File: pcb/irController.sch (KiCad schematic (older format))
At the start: 29 parts, among them J1 B4B-PH-K-S(LF)(SN), P1 ZX62R-B-5P, P2 GPIO_USER, Q1 Q_NMOS, SW1 SKRPACE010, SW2 SKRPACE010, U1 NJM2845, U2 ESP-13-WROOM-02, U3 IRSNS_GP1UXC41QS

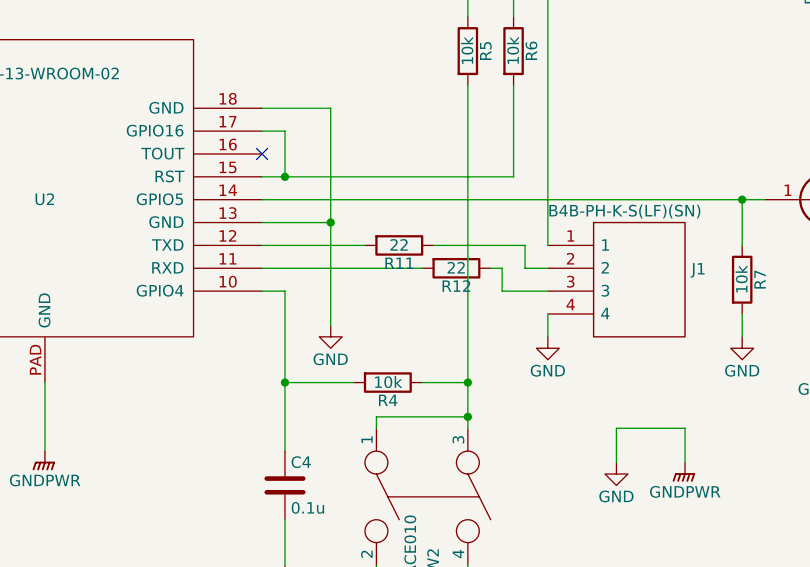
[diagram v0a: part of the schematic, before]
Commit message: 通信線の誤配線を修正
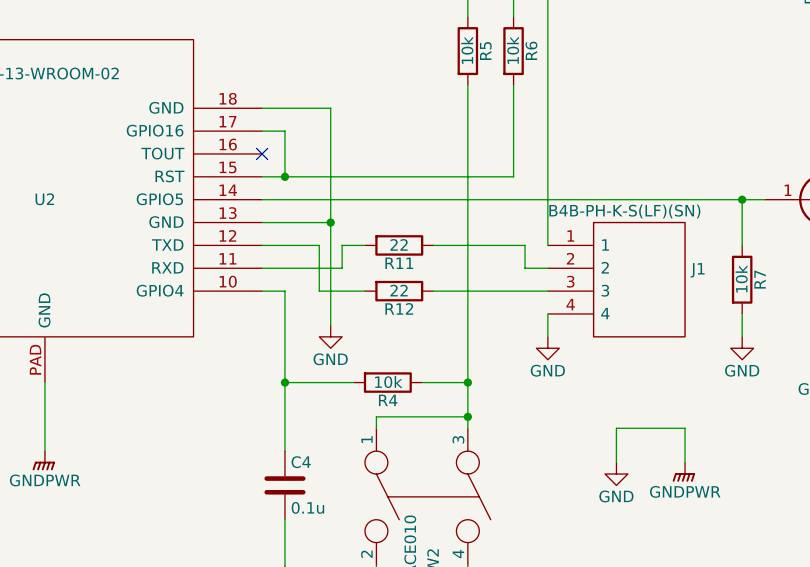
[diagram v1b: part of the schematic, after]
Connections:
- wire segments 115 -> 117
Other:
- moved on the sheet: R12
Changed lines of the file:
@@
 	6900 3600 9000 3600
-Wire Wire Line
-	6900 3900 7600 3900
 Wire Wire Line
 	2850 3200 2900 3200
@@
 $EndComp
 Wire Wire Line
-	8150 4000 7950 4000
-Wire Wire Line
-	7950 4000 7950 3900
-Wire Wire Line
 	8150 3900 8050 3900
 Wire Wire Line
@@
 Wire Wire Line
 	7200 3700 7200 4150
-Wire Wire Line
-	6900 3800 7350 3800
 Wire Wire Line
 	7650 3800 8050 3800
@@
 	0    1    1    0
 $EndComp
-$Comp
-L irController-rescue:R R12
-U 1 1 5E13E423
-P 7750 3900
-F 0 "R12" V 7830 3900 50  0000 C CNN
-F 1 "22" V 7750 3900 50  0000 C CNN
-F 2 "Resistor_SMD:R_0603_1608Metric" V 7680 3900 50  0001 C CNN
-F 3 "" H 7750 3900 50  0000 C CNN
-	1    7750 3900
-	0    1    1    0
-$EndComp
-Wire Wire Line
-	7900 3900 7950 3900
 Wire Wire Line
 	7300 4400 7000 4400
@@
 Wire Wire Line
 	3750 3900 3350 3900
+Wire Wire Line
+	6900 3800 7150 3800
+$Comp
+L irController-rescue:R R12
+U 1 1 5E13E423
+P 7500 4000
+F 0 "R12" V 7580 4000 50  0000 C CNN
+F 1 "22" V 7500 4000 50  0000 C CNN
+F 2 "Resistor_SMD:R_0603_1608Metric" V 7430 4000 50  0001 C CNN
+F 3 "" H 7500 4000 50  0000 C CNN
+	1    7500 4000
+	0    1    1    0
+$EndComp
+Wire Wire Line
+	7650 4000 8150 4000
+Wire Wire Line
+	7150 4000 7350 4000
+Wire Wire Line
+	7150 3800 7150 4000
+Wire Wire Line
+	6900 3900 7250 3900
+Wire Wire Line
+	7250 3900 7250 3800
+Wire Wire Line
+	7250 3800 7350 3800
 $EndSCHEMATC

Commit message: 温度センサ搭載
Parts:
- removed P2: GPIO_USER, Socket_Strips:Socket_Strip_Straight_1x02, symbol irController-rescue:CONN_01X02
- added C5: 0.1u, Capacitors_SMD:C_0603, symbol irController-rescue:C
- added IC1: ADT7410TRZ, SOIC127P600X175-8N, symbol SamacSys:ADT7410TRZ
- added R14, R15, R16, R17: 10k, Resistor_SMD:R_0603_1608Metric, symbol irController-rescue:R
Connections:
- net labels added: +3V3
- wire segments 117 -> 151
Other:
- note added: "I2C Bus Address Options\nA0: L\nA1: L\naddress: 0x48"
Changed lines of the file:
@@
 	1    0    0    -1
-$EndComp
-$Comp
-L irController-rescue:CONN_01X02 P2
-U 1 1 585CF068
-P 4050 3550
-F 0 "P2" H 4050 3750 50  0000 C CNN
-F 1 "GPIO_USER" V 4150 3550 50  0000 C CNN
-F 2 "Socket_Strips:Socket_Strip_Straight_1x02" H 4050 3550 50  0001 C CNN
-F 3 "" H 4050 3550 50  0000 C CNN
-	1    4050 3550
-	-1   0    0    1
 $EndComp
 NoConn ~ 6900 3400
@@
 Connection ~ 9700 3350
 Wire Wire Line
-	3100 2300 7800 2300
-Wire Wire Line
 	9400 2300 9400 2500
 Connection ~ 8000 2300
@@
 	3650 3200 3650 3350
 Wire Wire Line
-	4250 3500 4950 3500
-Wire Wire Line
-	4950 3600 4250 3600
-Wire Wire Line
 	4400 4000 4400 3700
 Wire Wire Line
@@
 	7200 3200 7200 3700
 Wire Wire Line
-	3100 3200 3100 2300
+	3100 3200 3100 2900
 Connection ~ 3100 3200
 Wire Wire Line
@@
 Wire Wire Line
 	7800 2800 7800 2300
-Connection ~ 7800 2300
 Wire Wire Line
 	7800 3100 7800 4400
@@
 Wire Wire Line
 	7000 3500 8000 3500
-Wire Wire Line
-	3650 3200 4500 3200
 Wire Wire Line
 	3350 3900 3350 4000
@@
 Wire Wire Line
 	7250 3800 7350 3800
+$Comp
+L SamacSys:ADT7410TRZ IC1
+U 1 1 5E806B94
+P 4550 1600
+F 0 "IC1" H 5050 1865 50  0000 C CNN
+F 1 "ADT7410TRZ" H 5050 1774 50  0000 C CNN
+F 2 "SOIC127P600X175-8N" H 5400 1700 50  0001 L CNN
+F 3 "http://componentsearchengine.com/Datasheets/3/ADT7410TRZ.pdf" H 5400 1600 50  0001 L CNN
+F 4 "I2C Temperature Sensor" H 5400 1500 50  0001 L CNN "Description"
+F 5 "1.75" H 5400 1400 50  0001 L CNN "Height"
+F 6 "Analog Devices" H 5400 1300 50  0001 L CNN "Manufacturer_Name"
+F 7 "ADT7410TRZ" H 5400 1200 50  0001 L CNN "Manufacturer_Part_Number"
+F 8 "584-ADT7410TRZ" H 5400 1100 50  0001 L CNN "Mouser Part Number"
+F 9 "https://www.mouser.com/Search/Refine.aspx?Keyword=584-ADT7410TRZ" H 5400 1000 50  0001 L CNN "Mouser Price/Stock"
+F 10 "7591890P" H 5400 900 50  0001 L CNN "RS Part Number"
+F 11 "http://uk.rs-online.com/web/p/products/7591890P" H 5400 800 50  0001 L CNN "RS Price/Stock"
+	1    4550 1600
+	1    0    0    -1
+$EndComp
+Wire Wire Line
+	5550 1700 5950 1700
+Wire Wire Line
+	3650 3200 4500 3200
+Wire Wire Line
+	3850 1600 3850 3600
+Wire Wire Line
+	3850 3600 4950 3600
+Wire Wire Line
+	3950 1700 3950 3500
+Wire Wire Line
+	3950 3500 4950 3500
+$Comp
+L power:+3V3 #PWR0101
+U 1 1 5E82A6D6
+P 3100 2900
+F 0 "#PWR0101" H 3100 2750 50  0001 C CNN
+F 1 "+3V3" H 3115 3073 50  0000 C CNN
+F 2 "" H 3100 2900 50  0001 C CNN
+F 3 "" H 3100 2900 50  0001 C CNN
+	1    3100 2900
+	1    0    0    -1
+$EndComp
+$Comp
+L power:+3V3 #PWR0102
+U 1 1 5E82BE3B
+P 7800 2050
+F 0 "#PWR0102" H 7800 1900 50  0001 C CNN
+F 1 "+3V3" H 7815 2223 50  0000 C CNN
+F 2 "" H 7800 2050 50  0001 C CNN
+F 3 "" H 7800 2050 50  0001 C CNN
+	1    7800 2050
+	1    0    0    -1
+$EndComp
+$Comp
+L power:+3V3 #PWR0103
+U 1 1 5E82C6A0
+P 6000 900
+F 0 "#PWR0103" H 6000 750 50  0001 C CNN
+F 1 "+3V3" H 6015 1073 50  0000 C CNN
+F 2 "" H 6000 900 50  0001 C CNN
+F 3 "" H 6000 900 50  0001 C CNN
+	1    6000 900
+	1    0    0    -1
+$EndComp
+Wire Wire Line
+	7800 2050 7800 2300
+Connection ~ 7800 2300
+$Comp
+L irController-rescue:GND #PWR0104
+U 1 1 5E835B5C
+P 5950 2000
+F 0 "#PWR0104" H 5950 1750 50  0001 C CNN
+F 1 "GND" H 5950 1850 50  0000 C CNN
+F 2 "" H 5950 2000 50  0000 C CNN
+F 3 "" H 5950 2000 50  0000 C CNN
+	1    5950 2000
+	1    0    0    -1
+$EndComp
+Wire Wire Line
+	5950 1700 5950 1950
+$Comp
+L irController-rescue:C C5
+U 1 1 5E8551FE
+P 6250 1750
+F 0 "C5" H 6275 1850 50  0000 L CNN
+F 1 "0.1u" H 6275 1650 50  0000 L CNN
+F 2 "Capacitors_SMD:C_0603" H 6288 1600 50  0001 C CNN
+F 3 "" H 6250 1750 50  0000 C CNN
+	1    6250 1750
+	1    0    0    -1
+$EndComp
+Wire Wire Line
+	6250 1900 6250 1950
+Wire Wire Line
+	6250 1950 5950 1950
+Connection ~ 5950 1950
+Wire Wire Line
+	5950 1950 5950 2000
+Wire Wire Line
+	5550 1600 6000 1600
+Wire Wire Line
+	6000 900  6000 1000
+Connection ~ 6000 1600
+Wire Wire Line
+	6000 1600 6250 1600
+$Comp
+L irController-rescue:GND #PWR0105
+U 1 1 5E873BF2
+P 4250 2100
+F 0 "#PWR0105" H 4250 1850 50  0001 C CNN
+F 1 "GND" H 4250 1950 50  0000 C CNN
+F 2 "" H 4250 2100 50  0000 C CNN
+F 3 "" H 4250 2100 50  0000 C CNN
+	1    4250 2100
+	1    0    0    -1
+$EndComp
+Wire Wire Line
+	4550 1800 4250 1800
+Wire Wire Line
+	4250 1800 4250 1900
+Wire Wire Line
+	4550 1900 4250 1900
+Connection ~ 4250 1900
+Wire Wire Line
+	4250 1900 4250 2100
+Text Notes 4500 1250 0    50   ~ 0
+I2C Bus Address Options\nA0: L\nA1: L\naddress: 0x48
+Connection ~ 4250 1700
+Connection ~ 4000 1600
+Wire Wire Line
+	4250 1700 3950 1700
+Wire Wire Line
+	4550 1700 4250 1700
+Wire Wire Line
+	4000 1600 3850 1600
+Wire Wire Line
+	4550 1600 4000 1600
+Wire Wire Line
+	4000 1100 4000 1200
+Connection ~ 4000 1100
+Wire Wire Line
+	4250 1100 4250 1200
+Wire Wire Line
+	4000 1100 4250 1100
+Wire Wire Line
+	4000 1000 4000 1100
+$Comp
+L power:+3V3 #PWR0106
+U 1 1 5E84A991
+P 4000 1000
+F 0 "#PWR0106" H 4000 850 50  0001 C CNN
+F 1 "+3V3" H 4015 1173 50  0000 C CNN
+F 2 "" H 4000 1000 50  0001 C CNN
+F 3 "" H 4000 1000 50  0001 C CNN
+	1    4000 1000
+	1    0    0    -1
+$EndComp
+Wire Wire Line
+	4250 1500 4250 1700
+Wire Wire Line
+	4000 1500 4000 1600
+$Comp
+L irController-rescue:R R15
+U 1 1 5E840B76
+P 4250 1350
+F 0 "R15" V 4330 1350 50  0000 C CNN
+F 1 "10k" V 4250 1350 50  0000 C CNN
+F 2 "Resistor_SMD:R_0603_1608Metric" V 4180 1350 50  0001 C CNN
+F 3 "" H 4250 1350 50  0000 C CNN
+	1    4250 1350
+	1    0    0    -1
+$EndComp
+$Comp
+L irController-rescue:R R14
+U 1 1 5E83AB10
+P 4000 1350
+F 0 "R14" V 4080 1350 50  0000 C CNN
+F 1 "10k" V 4000 1350 50  0000 C CNN
+F 2 "Resistor_SMD:R_0603_1608Metric" V 3930 1350 50  0001 C CNN
+F 3 "" H 4000 1350 50  0000 C CNN
+	1    4000 1350
+	1    0    0    -1
+$EndComp
+$Comp
+L irController-rescue:R R16
+U 1 1 5E893838
+P 5600 1300
+F 0 "R16" V 5680 1300 50  0000 C CNN
+F 1 "10k" V 5600 1300 50  0000 C CNN
+F 2 "Resistor_SMD:R_0603_1608Metric" V 5530 1300 50  0001 C CNN
+F 3 "" H 5600 1300 50  0000 C CNN
+	1    5600 1300
+	1    0    0    -1
+$EndComp
+$Comp
+L irController-rescue:R R17
+U 1 1 5E893E34
+P 5800 1300
+F 0 "R17" V 5880 1300 50  0000 C CNN
+F 1 "10k" V 5800 1300 50  0000 C CNN
+F 2 "Resistor_SMD:R_0603_1608Metric" V 5730 1300 50  0001 C CNN
+F 3 "" H 5800 1300 50  0000 C CNN
+	1    5800 1300
+	1    0    0    -1
+$EndComp
+Wire Wire Line
+	6000 1000 5600 1000
+Wire Wire Line
+	5600 1000 5600 1150
+Connection ~ 6000 1000
+Wire Wire Line
+	6000 1000 6000 1100
+Wire Wire Line
+	6000 1100 5800 1100
+Wire Wire Line
+	5800 1100 5800 1150
+Connection ~ 6000 1100
+Wire Wire Line
+	6000 1100 6000 1600
+Wire Wire Line
+	5600 1450 5600 1800
+Wire Wire Line
+	5600 1800 5550 1800
+Wire Wire Line
+	5550 1900 5800 1900
+Wire Wire Line
+	5800 1900 5800 1450
 $EndSCHEMATC

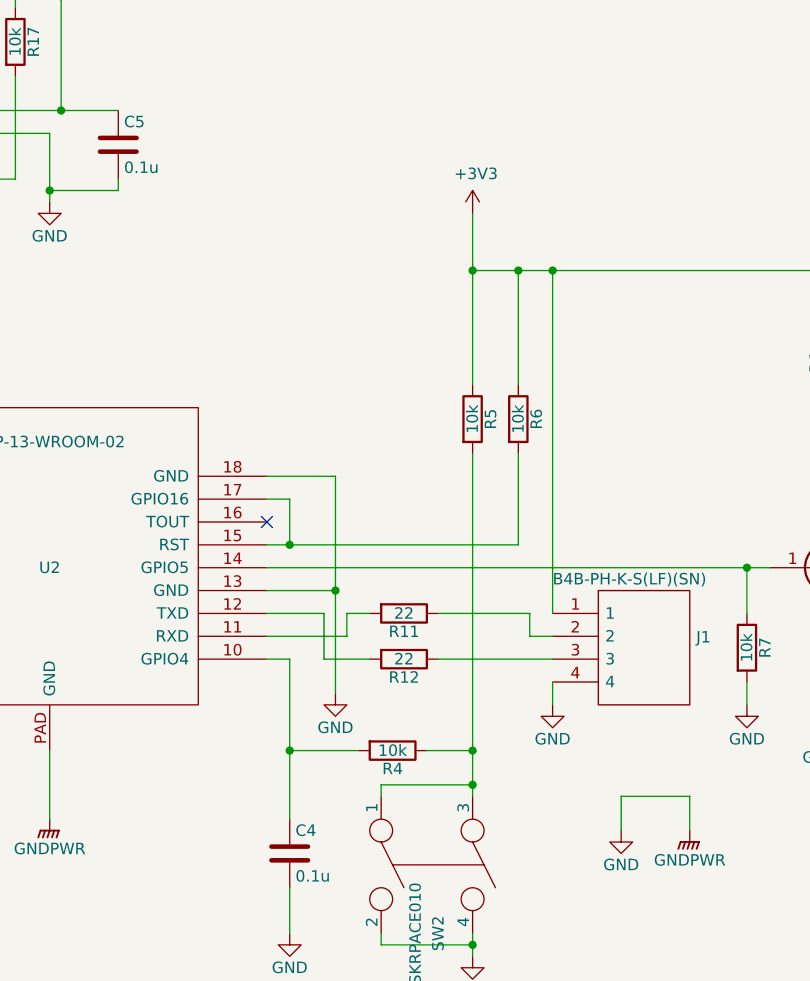
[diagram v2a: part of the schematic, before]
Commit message: ユーザ用ボタンをリセットボタンに変更
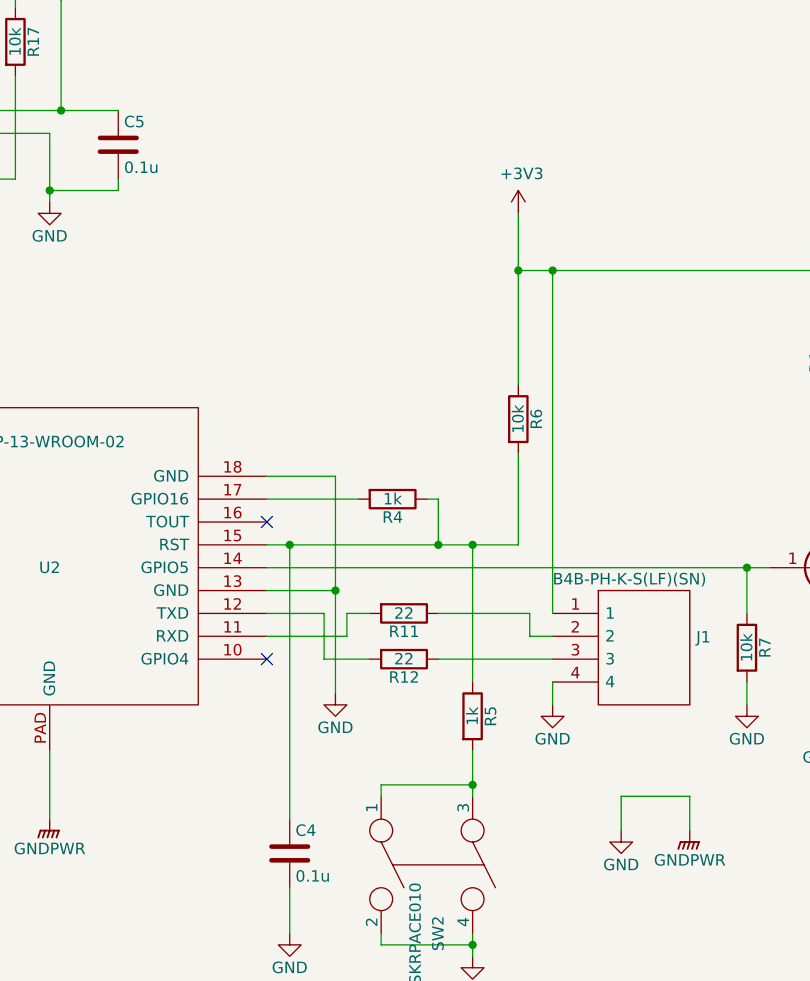
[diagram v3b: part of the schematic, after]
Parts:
- R4, R5: value 10k -> 1k
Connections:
- net +3V3: no longer R5.1
- net at R6.2, U2.15 (RST): now also C4.1, R4.1, R5.1; no longer U2.17 (GPIO16)
- net at R5.2, SW2.1, SW2.3: no longer R4.1
- new net: R4.2, U2.17 (GPIO16)
- now unconnected: U2.10 (GPIO4)
- no-connect marks 4 -> 5
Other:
- moved on the sheet: R5
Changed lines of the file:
@@
 L irController-rescue:R R5
 U 1 1 585D6283
-P 7800 2950
-F 0 "R5" V 7880 2950 50  0000 C CNN
-F 1 "10k" V 7800 2950 50  0000 C CNN
-F 2 "Resistor_SMD:R_0603_1608Metric" V 7730 2950 50  0001 C CNN
-F 3 "" H 7800 2950 50  0000 C CNN
-	1    7800 2950
+P 7800 4250
+F 0 "R5" V 7880 4250 50  0000 C CNN
+F 1 "1k" V 7800 4250 50  0000 C CNN
+F 2 "Resistor_SMD:R_0603_1608Metric" V 7730 4250 50  0001 C CNN
+F 3 "" H 7800 4250 50  0000 C CNN
+	1    7800 4250
 	1    0    0    -1
 $EndComp
@@
 	1    7000 4850
 	1    0    0    -1
-$EndComp
-$Comp
-L irController-rescue:R R4
-U 1 1 585D8CA6
-P 7450 4400
-F 0 "R4" V 7530 4400 50  0000 C CNN
-F 1 "10k" V 7450 4400 50  0000 C CNN
-F 2 "Resistor_SMD:R_0603_1608Metric" V 7380 4400 50  0001 C CNN
-F 3 "" H 7450 4400 50  0000 C CNN
-	1    7450 4400
-	0    1    1    0
 $EndComp
 $Comp
@@
 	8000 3500 8000 3100
 Wire Wire Line
-	6900 3500 7000 3500
-Wire Wire Line
-	6900 3300 7000 3300
-Wire Wire Line
 	9400 3300 9400 3350
 Wire Wire Line
@@
 Wire Wire Line
 	9400 2300 9400 2500
-Connection ~ 8000 2300
 Wire Wire Line
 	9700 2300 9700 2500
@@
 Wire Wire Line
 	10000 2900 10000 3000
-Wire Wire Line
-	7000 3300 7000 3500
-Connection ~ 7000 3500
 Wire Wire Line
 	7200 3200 6900 3200
@@
 Connection ~ 1900 3200
 Wire Wire Line
-	6900 4000 7000 4000
-Wire Wire Line
 	7800 5200 7800 5250
 Wire Wire Line
@@
 Connection ~ 4400 4450
 Wire Wire Line
-	7000 4000 7000 4400
-Wire Wire Line
 	7000 5000 7000 5200
-Wire Wire Line
-	7800 2800 7800 2300
-Wire Wire Line
-	7800 3100 7800 4400
-Wire Wire Line
-	7800 4400 7600 4400
-Connection ~ 7800 4400
 Wire Wire Line
 	9000 3800 9000 3600
@@
 	4800 3200 4950 3200
 Wire Wire Line
-	7000 3500 8000 3500
-Wire Wire Line
 	3350 3900 3350 4000
 Wire Wire Line
@@
 Wire Wire Line
 	4400 4450 4400 4550
-Wire Wire Line
-	7800 2300 8000 2300
-Wire Wire Line
-	7800 4400 7800 4550
 Wire Wire Line
 	9000 3600 9100 3600
@@
 	0    1    1    0
 $EndComp
-Wire Wire Line
-	7300 4400 7000 4400
-Connection ~ 7000 4400
-Wire Wire Line
-	7000 4400 7000 4700
 $Comp
 L irController-rescue:ESP-13-WROOM-02 U2
@@
 L power:+3V3 #PWR0102
 U 1 1 5E82BE3B
-P 7800 2050
-F 0 "#PWR0102" H 7800 1900 50  0001 C CNN
-F 1 "+3V3" H 7815 2223 50  0000 C CNN
-F 2 "" H 7800 2050 50  0001 C CNN
-F 3 "" H 7800 2050 50  0001 C CNN
-	1    7800 2050
+P 8000 2050
+F 0 "#PWR0102" H 8000 1900 50  0001 C CNN
+F 1 "+3V3" H 8015 2223 50  0000 C CNN
+F 2 "" H 8000 2050 50  0001 C CNN
+F 3 "" H 8000 2050 50  0001 C CNN
+	1    8000 2050
 	1    0    0    -1
 $EndComp
@@
 $EndComp
 Wire Wire Line
-	7800 2050 7800 2300
-Connection ~ 7800 2300
+	8000 2050 8000 2300
 $Comp
 L irController-rescue:GND #PWR0104
@@
 Wire Wire Line
 	5800 1900 5800 1450
+NoConn ~ 6900 4000
+$Comp
+L irController-rescue:R R4
+U 1 1 5E811C8F
+P 7450 3300
+F 0 "R4" V 7530 3300 50  0000 C CNN
+F 1 "1k" V 7450 3300 50  0000 C CNN
+F 2 "Resistor_SMD:R_0603_1608Metric" V 7380 3300 50  0001 C CNN
+F 3 "" H 7450 3300 50  0000 C CNN
+	1    7450 3300
+	0    1    1    0
+$EndComp
+Wire Wire Line
+	6900 3300 7300 3300
+Wire Wire Line
+	7000 4700 7000 3500
+Wire Wire Line
+	6900 3500 7000 3500
+Connection ~ 7000 3500
+Wire Wire Line
+	7800 4400 7800 4550
+Wire Wire Line
+	7000 3500 7650 3500
+Wire Wire Line
+	7800 4100 7800 3500
+Connection ~ 7800 3500
+Wire Wire Line
+	7800 3500 8000 3500
+Wire Wire Line
+	7600 3300 7650 3300
+Wire Wire Line
+	7650 3300 7650 3500
+Connection ~ 7650 3500
+Wire Wire Line
+	7650 3500 7800 3500
+Connection ~ 8000 2300
 $EndSCHEMATC

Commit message: LEDの電源電圧を選択できるようにした
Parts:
- added JP1: SolderJumper_3_Open, Jumper:SolderJumper-3_P1.3mm_Open_RoundedPad1.0x1.5mm_NumberLabels, symbol Jumper:SolderJumper_3_Open
- IC1: footprint SOIC127P600X175-8N -> SamacSys:SOIC127P600X175-8N
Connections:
- net +3V3: now also JP1.1 (A); no longer D1.2 (A), D2.2 (A), D3.2 (A)
- net +5V: now reaches C1.1, P1.1 (VCC), U1.VI
- net +5V: now also JP1.3 (B)
- new net: D1.2 (A), D2.2 (A), D3.2 (A), JP1.2 (C)
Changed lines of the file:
@@
 Wire Wire Line
 	9700 2300 9700 2500
-Connection ~ 9400 2300
 Wire Wire Line
 	10000 2300 10000 2500
@@
 	1900 3200 1900 3400
 Wire Wire Line
-	1550 3200 1900 3200
+	1550 3200 1700 3200
 Connection ~ 1900 3200
 Wire Wire Line
@@
 Wire Wire Line
 	8150 3800 8150 2300
-Connection ~ 8150 2300
-Wire Wire Line
-	8150 2300 9400 2300
 Wire Wire Line
 	7200 3700 7200 4150
@@
 F 0 "IC1" H 5050 1865 50  0000 C CNN
 F 1 "ADT7410TRZ" H 5050 1774 50  0000 C CNN
-F 2 "SOIC127P600X175-8N" H 5400 1700 50  0001 L CNN
+F 2 "SamacSys:SOIC127P600X175-8N" H 5400 1700 50  0001 L CNN
 F 3 "http://componentsearchengine.com/Datasheets/3/ADT7410TRZ.pdf" H 5400 1600 50  0001 L CNN
 F 4 "I2C Temperature Sensor" H 5400 1500 50  0001 L CNN "Description"
@@
 	7650 3500 7800 3500
 Connection ~ 8000 2300
+$Comp
+L Jumper:SolderJumper_3_Open JP1
+U 1 1 5E8354F2
+P 9400 1800
+F 0 "JP1" H 9400 2005 50  0000 C CNN
+F 1 "SolderJumper_3_Open" H 9400 1914 50  0000 C CNN
+F 2 "Jumper:SolderJumper-3_P1.3mm_Open_RoundedPad1.0x1.5mm_NumberLabels" H 9400 1800 50  0001 C CNN
+F 3 "~" H 9400 1800 50  0001 C CNN
+	1    9400 1800
+	1    0    0    -1
+$EndComp
+$Comp
+L power:+5V #PWR0107
+U 1 1 5E83656A
+P 1700 3050
+F 0 "#PWR0107" H 1700 2900 50  0001 C CNN
+F 1 "+5V" H 1715 3223 50  0000 C CNN
+F 2 "" H 1700 3050 50  0001 C CNN
+F 3 "" H 1700 3050 50  0001 C CNN
+	1    1700 3050
+	1    0    0    -1
+$EndComp
+Wire Wire Line
+	1700 3050 1700 3200
+Connection ~ 1700 3200
+Wire Wire Line
+	1700 3200 1900 3200
+Wire Wire Line
+	9400 1950 9400 2300
+Connection ~ 9400 2300
+Wire Wire Line
+	9200 1800 8800 1800
+Wire Wire Line
+	8800 1800 8800 1450
+$Comp
+L power:+3V3 #PWR0108
+U 1 1 5E84B46E
+P 8800 1450
+F 0 "#PWR0108" H 8800 1300 50  0001 C CNN
+F 1 "+3V3" H 8815 1623 50  0000 C CNN
+F 2 "" H 8800 1450 50  0001 C CNN
+F 3 "" H 8800 1450 50  0001 C CNN
+	1    8800 1450
+	1    0    0    -1
+$EndComp
+$Comp
+L power:+5V #PWR0109
+U 1 1 5E84B8AF
+P 10050 1400
+F 0 "#PWR0109" H 10050 1250 50  0001 C CNN
+F 1 "+5V" H 10065 1573 50  0000 C CNN
+F 2 "" H 10050 1400 50  0001 C CNN
+F 3 "" H 10050 1400 50  0001 C CNN
+	1    10050 1400
+	1    0    0    -1
+$EndComp
+Wire Wire Line
+	9600 1800 10050 1800
+Wire Wire Line
+	10050 1800 10050 1400
 $EndSCHEMATC

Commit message: パターン引いた
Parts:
- C1, C2: footprint Capacitors_SMD:C_1206 -> Capacitor_SMD:C_1206_3216Metric
- C3: value 0.22u -> 0.1u; footprint Capacitors_SMD:C_0603 -> Capacitor_SMD:C_0603_1608Metric
- C4, C5: footprint Capacitors_SMD:C_0603 -> Capacitor_SMD:C_0603_1608Metric
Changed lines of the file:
@@
 F 0 "C1" H 1925 3650 50  0000 L CNN
 F 1 "22u" H 1925 3450 50  0000 L CNN
-F 2 "Capacitors_SMD:C_1206" H 1938 3400 50  0001 C CNN
+F 2 "Capacitor_SMD:C_1206_3216Metric" H 1938 3400 50  0001 C CNN
 F 3 "" H 1900 3550 50  0000 C CNN
 	1    1900 3550
@@
 F 0 "C2" H 2925 3650 50  0000 L CNN
 F 1 "22u" H 2925 3450 50  0000 L CNN
-F 2 "Capacitors_SMD:C_1206" H 2938 3400 50  0001 C CNN
+F 2 "Capacitor_SMD:C_1206_3216Metric" H 2938 3400 50  0001 C CNN
 F 3 "" H 2900 3550 50  0000 C CNN
 	1    2900 3550
@@
 F 0 "C4" H 7025 4950 50  0000 L CNN
 F 1 "0.1u" H 7025 4750 50  0000 L CNN
-F 2 "Capacitors_SMD:C_0603" H 7038 4700 50  0001 C CNN
+F 2 "Capacitor_SMD:C_0603_1608Metric" H 7038 4700 50  0001 C CNN
 F 3 "" H 7000 4850 50  0000 C CNN
 	1    7000 4850
@@
 P 4700 4350
 F 0 "C3" H 4725 4450 50  0000 L CNN
-F 1 "0.22u" H 4725 4250 50  0000 L CNN
-F 2 "Capacitors_SMD:C_0603" H 4738 4200 50  0001 C CNN
+F 1 "0.1u" H 4725 4250 50  0000 L CNN
+F 2 "Capacitor_SMD:C_0603_1608Metric" H 4738 4200 50  0001 C CNN
 F 3 "" H 4700 4350 50  0000 C CNN
 	1    4700 4350
@@
 F 0 "C5" H 6275 1850 50  0000 L CNN
 F 1 "0.1u" H 6275 1650 50  0000 L CNN
-F 2 "Capacitors_SMD:C_0603" H 6288 1600 50  0001 C CNN
+F 2 "Capacitor_SMD:C_0603_1608Metric" H 6288 1600 50  0001 C CNN
 F 3 "" H 6250 1750 50  0000 C CNN
 	1    6250 1750
